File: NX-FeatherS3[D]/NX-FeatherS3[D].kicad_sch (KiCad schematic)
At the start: 3 parts, among them J2 Right-Side, J3 Left-Side, J5 Conn_01x02_Pin

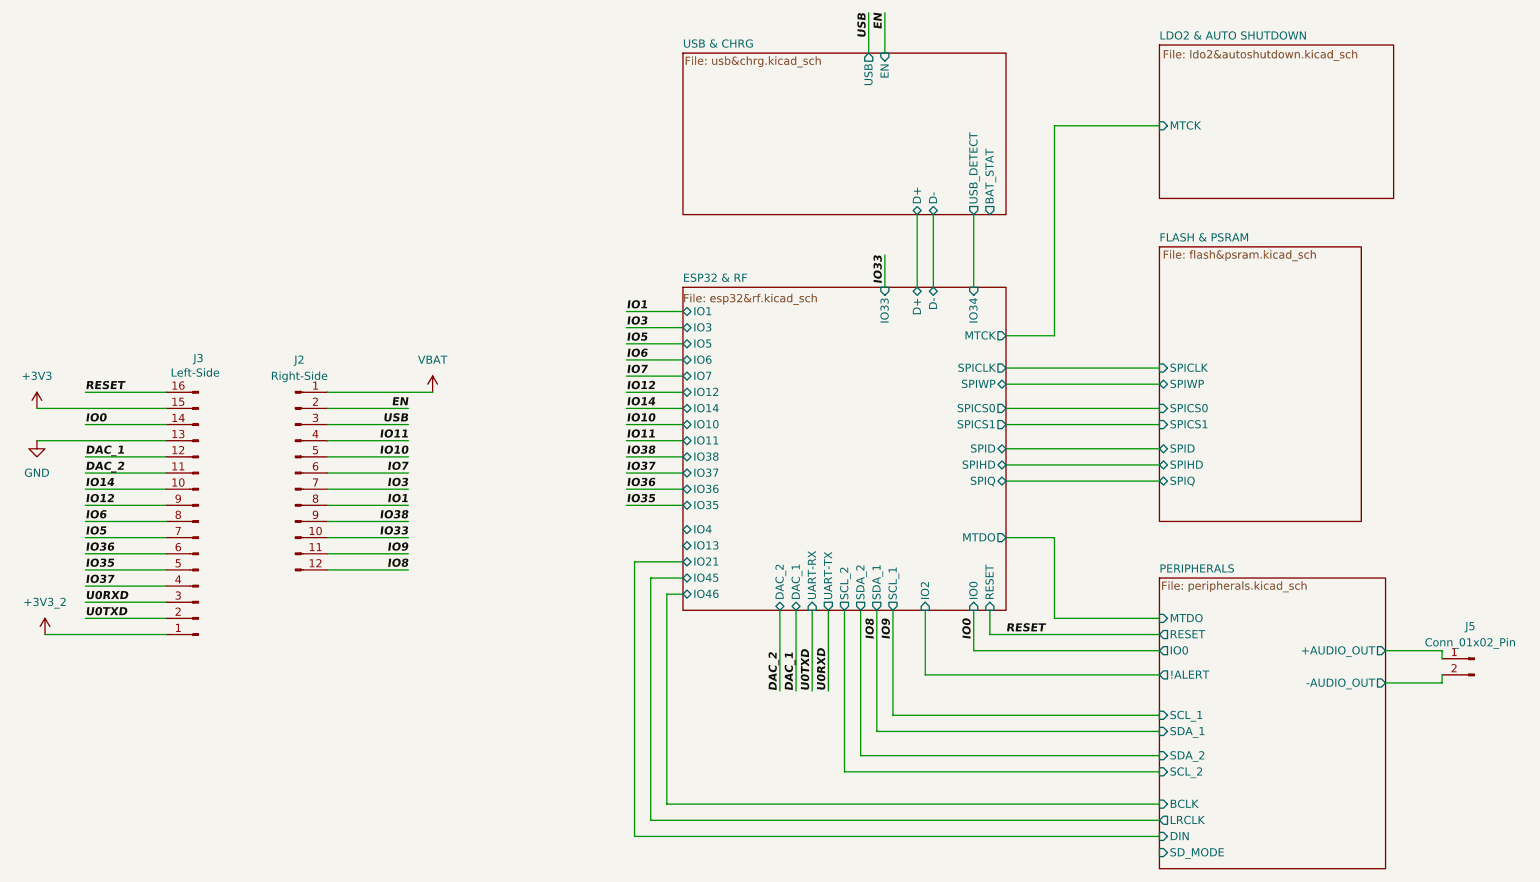
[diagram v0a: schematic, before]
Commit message: Added v1p0, updated Version
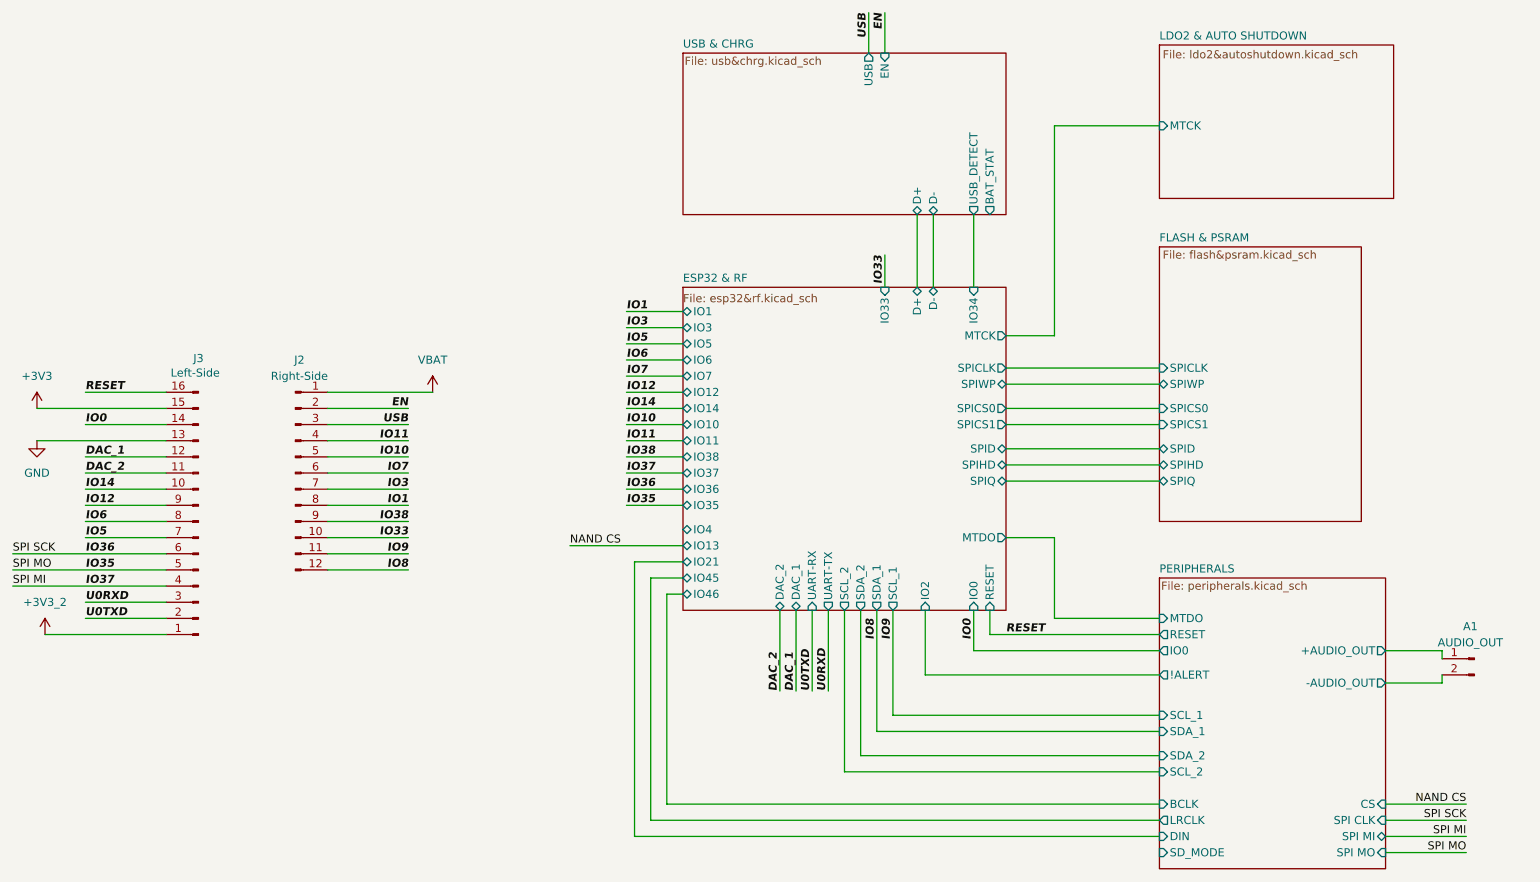
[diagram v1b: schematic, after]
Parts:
- A1: renamed from J5; value Conn_01x02_Pin -> AUDIO_OUT
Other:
- sheet PERIPHERALS ports: added CS, SPI CLK, SPI MI, SPI MO; removed none
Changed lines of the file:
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@@
+	(wire
+		(pts
+			(xy 259.08 152.4) (xy 271.78 152.4)
+		)
+		(stroke
+			(width 0)
+			(type default)
+		)
+	)
 	(wire
 		(pts
@@
 	(wire
 		(pts
+			(xy 43.18 110.49) (xy 67.31 110.49)
+		)
+		(stroke
+			(width 0)
+			(type default)
+		)
+	)
+	(wire
+		(pts
 			(xy 187.96 52.07) (xy 187.96 63.5)
 		)
@@
 	(wire
 		(pts
-			(xy 67.31 107.95) (xy 54.61 107.95)
-		)
-		(stroke
-			(width 0)
-			(type default)
-		)
-	)
-	(wire
-		(pts
 			(xy 207.01 38.1) (xy 207.01 71.12)
 		)
@@
 	(wire
 		(pts
+			(xy 43.18 107.95) (xy 67.31 107.95)
+		)
+		(stroke
+			(width 0)
+			(type default)
+		)
+	)
+	(wire
+		(pts
 			(xy 267.97 120.65) (xy 267.97 121.92)
 		)
@@
 	(wire
 		(pts
-			(xy 67.31 105.41) (xy 54.61 105.41)
-		)
-		(stroke
-			(width 0)
-			(type default)
-		)
-	)
-	(wire
-		(pts
 			(xy 180.34 58.42) (xy 180.34 63.5)
 		)
@@
 	(wire
 		(pts
+			(xy 259.08 149.86) (xy 271.78 149.86)
+		)
+		(stroke
+			(width 0)
+			(type default)
+		)
+	)
+	(wire
+		(pts
 			(xy 223.52 124.46) (xy 186.69 124.46)
 		)
@@
 	(wire
 		(pts
+			(xy 43.18 105.41) (xy 67.31 105.41)
+		)
+		(stroke
+			(width 0)
+			(type default)
+		)
+	)
+	(wire
+		(pts
+			(xy 130.81 104.14) (xy 148.59 104.14)
+		)
+		(stroke
+			(width 0)
+			(type default)
+		)
+	)
+	(wire
+		(pts
 			(xy 168.91 114.3) (xy 168.91 127)
 		)
@@
 	(wire
 		(pts
-			(xy 67.31 110.49) (xy 54.61 110.49)
+			(xy 259.08 144.78) (xy 271.78 144.78)
 		)
 		(stroke
@@
 		(pts
 			(xy 267.97 125.73) (xy 267.97 124.46)
+		)
+		(stroke
+			(width 0)
+			(type default)
+		)
+	)
+	(wire
+		(pts
+			(xy 259.08 147.32) (xy 271.78 147.32)
 		)
 		(stroke
@@
 		)
 	)
+	(label "SPI MI"
+		(at 43.18 110.49 0)
+		(effects
+			(font
+				(size 1.27 1.27)
+			)
+			(justify left bottom)
+		)
+	)
 	(label "IO7"
 		(at 139.7 77.47 0)
@@
 		)
 	)
+	(label "SPI MO"
+		(at 43.18 107.95 0)
+		(effects
+			(font
+				(size 1.27 1.27)
+			)
+			(justify left bottom)
+		)
+	)
 	(label "IO33"
 		(at 105.41 102.87 180)
@@
 		)
 	)
+	(label "SPI SCK"
+		(at 43.18 105.41 0)
+		(effects
+			(font
+				(size 1.27 1.27)
+			)
+			(justify left bottom)
+		)
+	)
 	(label "IO3"
 		(at 139.7 69.85 0)
@@
 		)
 	)
+	(label "SPI MI"
+		(at 271.78 149.86 180)
+		(effects
+			(font
+				(size 1.27 1.27)
+			)
+			(justify right bottom)
+		)
+	)
+	(label "SPI MO"
+		(at 271.78 152.4 180)
+		(effects
+			(font
+				(size 1.27 1.27)
+			)
+			(justify right bottom)
+		)
+	)
 	(label "U0RXD"
 		(at 171.45 127 90)
@@
 		)
 	)
+	(label "SPI SCK"
+		(at 271.78 147.32 180)
+		(effects
+			(font
+				(size 1.27 1.27)
+			)
+			(justify right bottom)
+		)
+	)
 	(label "IO3"
 		(at 105.41 95.25 180)
@@
 		)
 	)
+	(label "NAND CS"
+		(at 130.81 104.14 0)
+		(effects
+			(font
+				(size 1.27 1.27)
+			)
+			(justify left bottom)
+		)
+	)
 	(label "IO14"
 		(at 54.61 95.25 0)
@@
 			)
 			(justify left bottom)
+		)
+	)
+	(label "NAND CS"
+		(at 271.78 144.78 180)
+		(effects
+			(font
+				(size 1.27 1.27)
+			)
+			(justify right bottom)
 		)
 	)
@@
 		(on_board yes)
 		(dnp no)
-		(property "Reference" "J5"
+		(property "Reference" "A1"
 			(at 272.415 116.84 0)
 			(effects
@@
 			)
 		)
-		(property "Value" "Conn_01x02_Pin"
+		(property "Value" "AUDIO_OUT"
 			(at 272.415 119.38 0)
 			(effects
@@
 			(project ""
 				(path "/3e891cc2-3bbe-4423-b033-9519c2d66bb1"
-					(reference "J5")
+					(reference "A1")
 					(unit 1)
 				)
@@
 			)
 		)
+		(pin "CS" input
+			(at 259.08 144.78 0)
+			(effects
+				(font
+					(size 1.27 1.27)
+				)
+				(justify right)
+			)
+		)
+		(pin "SPI CLK" input
+			(at 259.08 147.32 0)
+			(effects
+				(font
+					(size 1.27 1.27)
+				)
+				(justify right)
+			)
+		)
+		(pin "SPI MI" tri_state
+			(at 259.08 149.86 0)
+			(effects
+				(font
+					(size 1.27 1.27)
+				)
+				(justify right)
+			)
+		)
+		(pin "SPI MO" input
+			(at 259.08 152.4 0)
+			(effects
+				(font
+					(size 1.27 1.27)
+				)
+				(justify right)
+			)
+		)
